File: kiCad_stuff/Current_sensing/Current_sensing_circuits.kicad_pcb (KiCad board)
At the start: 2 copper layers, 9.8 x 19 mm, 5 parts, among them J1 Conn_01x02, J2 Conn_01x03, U1 INA283

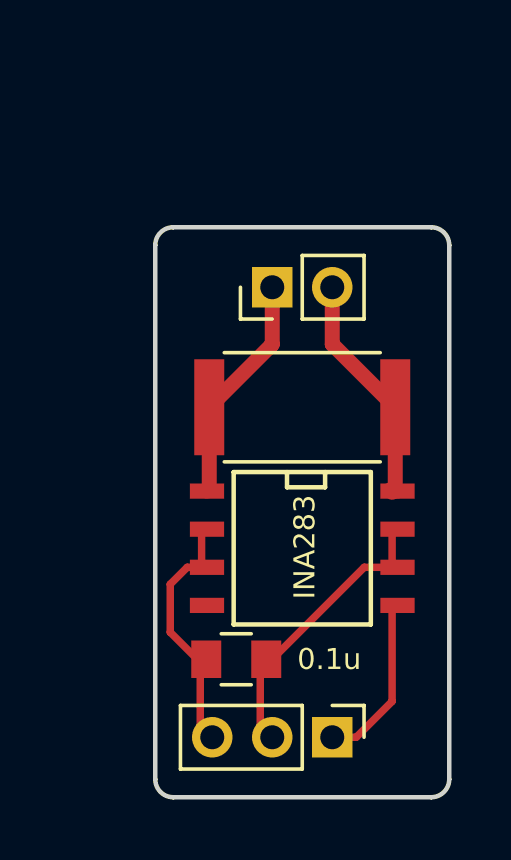
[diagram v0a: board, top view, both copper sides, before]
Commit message: 1mm trackwidth for shunt-resistor tracks
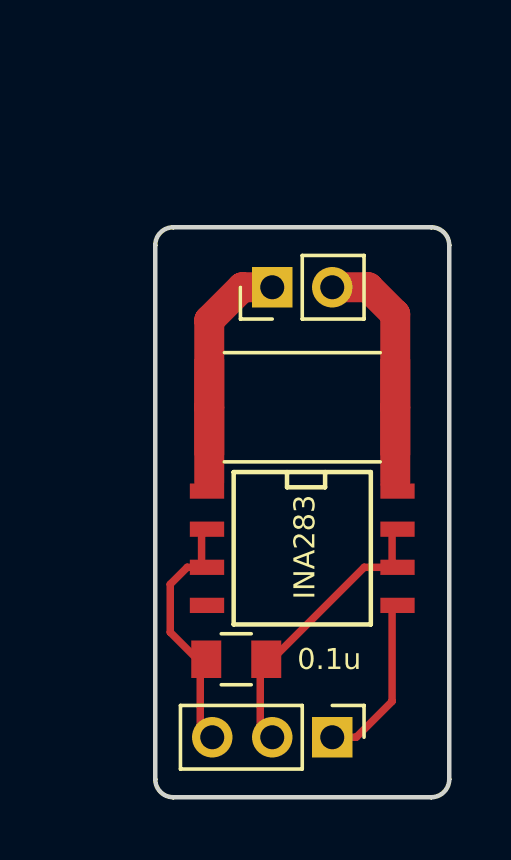
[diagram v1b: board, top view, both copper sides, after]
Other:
- net class PWR: clearance 0.3 -> 0.5; trace_width 0.5 -> 1
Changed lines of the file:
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@@
   (general
     (links 11)
-    (no_connects 0)
+    (no_connects 2)
     (area 136.024999 87.924999 145.975001 107.075001)
     (thickness 1.6)
     (drawings 14)
-    (tracks 26)
+    (tracks 25)
     (zones 0)
     (modules 5)
@@
   )
   (net_class PWR ""
-    (clearance 0.3)
-    (trace_width 0.5)
+    (clearance 0.5)
+    (trace_width 1)
     (via_dia 0.6)
     (via_drill 0.4)
@@
   (gr_line (start 145.9 92.1) (end 145.9 88) (angle 90) (layer Eco1.User) (width 0.2))
   (gr_line (start 136.1 106.9) (end 136.1 88.1) (angle 90) (layer Eco1.User) (width 0.2))
+  (segment (start 137.645 98.105) (end 137.645 99.375) (width 0.25) (layer F.Cu) (net 1))
   (segment (start 137.825 99.335) (end 137.165 99.335) (width 0.25) (layer F.Cu) (net 1))
   (segment (start 136.6 101.5) (end 137.7 102.6) (width 0.25) (layer F.Cu) (net 1))
@@
   (segment (start 137.6 102.7) (end 137.6 104.6) (width 0.25) (layer F.Cu) (net 1))
   (segment (start 137.6 104.6) (end 138 105) (width 0.25) (layer F.Cu) (net 1))
-  (segment (start 137.645 98.105) (end 137.645 99.375) (width 0.25) (layer F.Cu) (net 1))
+  (segment (start 143.995 98.105) (end 143.995 99.375) (width 0.25) (layer F.Cu) (net 2))
   (segment (start 139.8 102.4) (end 140 102.4) (width 0.25) (layer F.Cu) (net 2))
   (segment (start 140 102.4) (end 143.065 99.335) (width 0.25) (layer F.Cu) (net 2))
@@
   (segment (start 139.6 104.6) (end 140 105) (width 0.25) (layer F.Cu) (net 2))
   (segment (start 139.6 102.7) (end 139.7 102.7) (width 0.25) (layer F.Cu) (net 2))
-  (segment (start 143.995 98.105) (end 143.995 99.375) (width 0.25) (layer F.Cu) (net 2))
-  (segment (start 137.9 94) (end 137.9 96.72) (width 0.5) (layer F.Cu) (net 3))
-  (segment (start 137.9 96.72) (end 137.825 96.795) (width 0.5) (layer F.Cu) (net 3))
-  (segment (start 140 90) (end 140 91.9) (width 0.5) (layer F.Cu) (net 3))
-  (segment (start 140 91.9) (end 137.9 94) (width 0.5) (layer F.Cu) (net 3))
-  (segment (start 144.1 94) (end 144.1 96.72) (width 0.5) (layer F.Cu) (net 4))
-  (segment (start 144.1 96.72) (end 144.175 96.795) (width 0.5) (layer F.Cu) (net 4))
-  (segment (start 142 90) (end 142 91.9) (width 0.5) (layer F.Cu) (net 4))
-  (segment (start 142 91.9) (end 144.1 94) (width 0.5) (layer F.Cu) (net 4))
-  (segment (start 143.92 96.76) (end 143.995 96.835) (width 0.5) (layer F.Cu) (net 4))
+  (segment (start 137.9 94) (end 137.9 96.5) (width 1) (layer F.Cu) (net 3) (status 400000))
+  (segment (start 140 90) (end 139 90) (width 1) (layer F.Cu) (net 3))
+  (segment (start 137.9 91.1) (end 137.9 94) (width 1) (layer F.Cu) (net 3))
+  (segment (start 139 90) (end 137.9 91.1) (width 1) (layer F.Cu) (net 3))
+  (segment (start 144.1 94) (end 144.1 96.5) (width 1) (layer F.Cu) (net 4) (status 400000))
+  (segment (start 142 90) (end 143.2 90) (width 1) (layer F.Cu) (net 4))
+  (segment (start 144.1 90.9) (end 144.1 94) (width 1) (layer F.Cu) (net 4))
+  (segment (start 143.2 90) (end 144.1 90.9) (width 1) (layer F.Cu) (net 4))
   (segment (start 142 105) (end 142.8 105) (width 0.25) (layer F.Cu) (net 5))
   (segment (start 143.995 103.805) (end 143.995 100.645) (width 0.25) (layer F.Cu) (net 5))

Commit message: Added company logo to PCB library
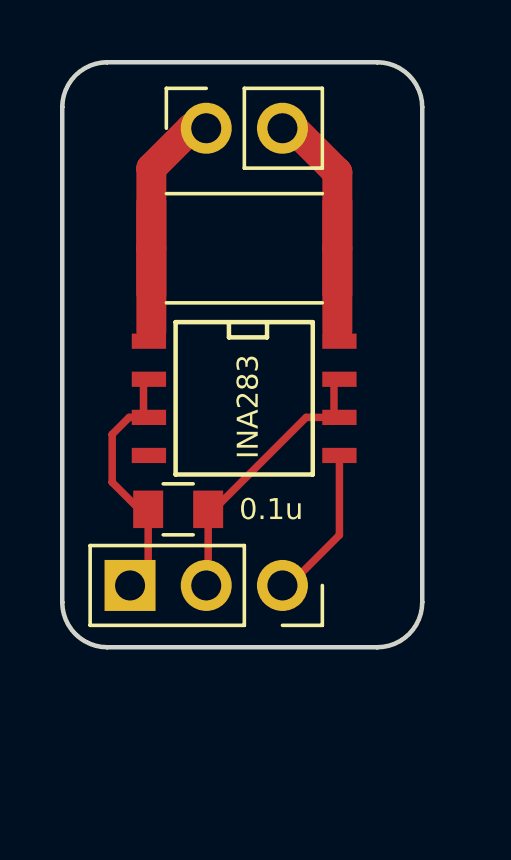
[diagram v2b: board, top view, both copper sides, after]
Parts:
- added G***: LOGO, AccessRoboticLtd_KiCadLib:logo, B.Cu at (139.0, 90.5)
- J1: footprint Pin_Headers:Pin_Header_Straight_1x02_Pitch2.00mm -> Connector_PinSocket_2.54mm:PinSocket_1x02_P2.54mm_Vertical
- J2: footprint Pin_Headers:Pin_Header_Straight_1x03_Pitch2.00mm -> Connector_PinSocket_2.54mm:PinSocket_1x03_P2.54mm_Vertical
- moved J1 5.74 mm to (137.8, 84.7)
- moved R_shunt1 5.64 mm to (139.1, 88.7)
- moved C_bypass1 5.36 mm to (136.9, 97.4)
- moved U1 5.36 mm to (139.1, 93.7)
- moved J2 5.33 mm to (140.3, 99.9)
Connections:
- U1 pad 4: Net-(U1-Pad4) -> (no net)
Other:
- board size 9.8 x 19 mm -> 12 x 19.5 mm
